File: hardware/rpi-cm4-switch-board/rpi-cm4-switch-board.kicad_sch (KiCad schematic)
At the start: 68 parts, among them J1 0826-1G1T-23-F, J2 0826-1G1T-23-F, J3 0826-1G1T-23-F, P1 USB_C_Plug_USB2.0, P2 USB_C_Plug_USB2.0, U3 74LVC1G07SE-7, U5 KSZ9567RTXI, U6 AP2127N-2.5, U7 AP2127N3-1.2

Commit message: Differential routing completed/roughed out. Schematic cleanup. More work to do on chip power pins.
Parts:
- removed CR1: SMBJ5.0A-TR, footprints:SMBJ5.0A-TR, symbol 2020-11-06_22-01-36:SMBJ5.0A-TR
- added C? (x27): 0.1uF, Capacitor_SMD:C_0402_1005Metric, symbol Device:C
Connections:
- net +3.3V: no longer U5.61 (VDDIO), U5.77 (VDDIO), U5.99 (VDDIO)
- net Cap5_D_P: now reaches C16.2, U5.120 (TXRX5P_D)
- net Cap5_C_P: now reaches C15.2, U5.117 (TXRX5P_C)
- net Cap4_C_N: now reaches C3.2, U5.40 (TXRX4M_C)
- net Cap4_B_P: now reaches C10.2, U5.37 (TXRX4P_B)
- net Cap5_A_N: now reaches C5.2, U5.113 (TXRX5M_A)
- net Cap4_D_N: now reaches C4.2, U5.43 (TXRX4M_D)
- net Cap5_A_P: now reaches C13.2, U5.112 (TXRX5P_A)
- net Cap4_A_N: now reaches C1.2, U5.35 (TXRX4M_A)
- net Cap4_C_P: now reaches C11.2, U5.39 (TXRX4P_C)
- net Cap5_C_N: now reaches C7.2, U5.118 (TXRX5M_C)
- net Cap5_B_P: now reaches C14.2, U5.115 (TXRX5P_B)
- net Cap5_B_N: now reaches C6.2, U5.116 (TXRX5M_B)
- net Cap5_D_N: now reaches C8.2, U5.121 (TXRX5M_D)
- net Cap4_A_P: now reaches C9.2, U5.34 (TXRX4P_A)
- net Cap4_B_N: now reaches C2.2, U5.38 (TXRX4M_B)
- net Cap4_D_P: now reaches C12.2, U5.42 (TXRX4P_D)
- net GPIO10: no longer names the net of Module2.44 (GPIO10)
- net GPIO10: no longer Module1.44 (GPIO10)
- net GPIO11: no longer names the net of Module2.38 (GPIO11)
- net GPIO11: no longer Module1.38 (GPIO11)
- net GPIO14: no longer names the net of Module2.55 (GPIO14)
- net GPIO14: no longer Module1.55 (GPIO14)
- net GPIO15: no longer names the net of Module2.51 (GPIO15)
- net GPIO15: no longer Module1.51 (GPIO15)
- net GPIO2: no longer names the net of Module2.58 (GPIO2)
- net GPIO2: no longer Module1.58 (GPIO2)
- net GPIO3: no longer names the net of Module2.56 (GPIO3)
- net GPIO3: no longer Module1.56 (GPIO3)
- net GPIO7: no longer names the net of Module2.37 (GPIO7)
- net GPIO7: no longer Module1.37 (GPIO7)
- net GPIO8: no longer names the net of Module2.39 (GPIO8)
- net GPIO8: no longer Module1.39 (GPIO8)
- net GPIO9: no longer names the net of Module2.40 (GPIO9)
- net GPIO9: no longer Module1.40 (GPIO9)
- now unconnected: U5.10 (AVDDH), U5.104 (DVDDL), U5.11 (DVDDL), U5.110 (DVDDL), U5.111 (AVDDH), U5.114 (AVDDL), U5.119 (AVDDL), U5.122 (AVDDH), U5.124 (AVDDL), U5.128 (AVDDH), U5.14 (AVDDL), U5.19 (AVDDL), U5.22 (AVDDH), U5.23 (DVDDL), U5.3 (AVDDL), U5.30 (AVDDL), U5.33 (AVDDH), U5.36 (AVDDL), U5.41 (AVDDL), U5.44 (AVDDH), U5.45 (DVDDL), U5.56 (DVDDL), U5.74 (DVDDL), U5.87 (DVDDL), U6.2 (VO), U7.2 (VO)
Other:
- moved on the sheet: C1, C10, C11, C12, C13, C14, C15, C16, C2, C3, C4, C5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

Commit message: Updated schematic symbol and footprint for ethernet chip, More work TBD
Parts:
- U? (x3): renamed from U5; value KSZ9567RTXI -> KSZ9567S; footprint library:QFP40P1600X1600X120-129N -> QFP40P1600X1600X120-129N; symbol KSZ9567RTXI:KSZ9567RTXI -> KSZ9567S:KSZ9567S
- gave numbers to parts that had none: 27
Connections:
- net +3.3V: now also U?.68 (VDDIO), U?.99 (VDDIO)
- net GND: now also U?.69 (GND), U?.75 (GND), U?.77 (GND), U?.80 (GND), U?.EPAD (GND); no longer U?.129 (GND), U?.46 (GND), U?.47 (GND), U?.84 (GND), U?.P1 (GND), U?.P10 (GND), U?.P11 (GND), U?.P12 (GND), U?.P13 (GND), U?.P14 (GND), U?.P15 (GND), U?.P16 (GND), U?.P17 (GND), U?.P18 (GND), U?.P19 (GND), U?.P2 (GND), U?.P20 (GND), U?.P21 (GND), U?.P22 (GND), U?.P23 (GND), U?.P24 (GND), U?.P25 (GND), U?.P26 (GND), U?.P27 (GND), U?.P28 (GND), U?.P29 (GND), U?.P3 (GND), U?.P30 (GND), U?.P31 (GND), U?.P32 (GND), U?.P33 (GND), U?.P34 (GND), U?.P35 (GND), U?.P36 (GND), U?.P37 (GND), U?.P38 (GND), U?.P39 (GND), U?.P4 (GND), U?.P40 (GND), U?.P41 (GND), U?.P42 (GND), U?.P43 (GND), U?.P44 (GND), U?.P45 (GND), U?.P48 (GND), U?.P49 (GND), U?.P5 (GND), U?.P50 (GND), U?.P51 (GND), U?.P52 (GND), U?.P53 (GND), U?.P54 (GND), U?.P55 (GND), U?.P56 (GND), U?.P57 (GND), U?.P58 (GND), U?.P59 (GND), U?.P6 (GND), U?.P60 (GND), U?.P61 (GND), U?.P62 (GND), U?.P63 (GND), U?.P64 (GND), U?.P7 (GND), U?.P8 (GND), U?.P9 (GND)
- net 1.2V: now reaches U7.2 (VO)
- net 1.2V: now also U?.104 (DVDDL), U?.11 (DVDDL), U?.110 (DVDDL), U?.114 (AVDDL), U?.119 (AVDDL), U?.124 (AVDDL), U?.14 (AVDDL), U?.19 (AVDDL), U?.23 (DVDDL), U?.3 (AVDDL), U?.30 (AVDDL), U?.36 (AVDDL), U?.41 (AVDDL), U?.45 (DVDDL), U?.56 (DVDDL), U?.66 (DVDDL), U?.70 (DVDDL), U?.71 (VDDLS), U?.84 (VDDLS), U?.87 (DVDDL)
- net 2.5V: now reaches U?.10 (AVDDH)
- net 2.5V: now also U6.2 (VO), U?.111 (AVDDH), U?.122 (AVDDH), U?.128 (AVDDH), U?.22 (AVDDH), U?.33 (AVDDH), U?.44 (AVDDH), U?.72 (VDDHS), U?.83 (VDDHS)
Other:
- moved on the sheet: C17, C18, C19, C20, C21, C22, C23, C24, C25, C26, C27, C28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

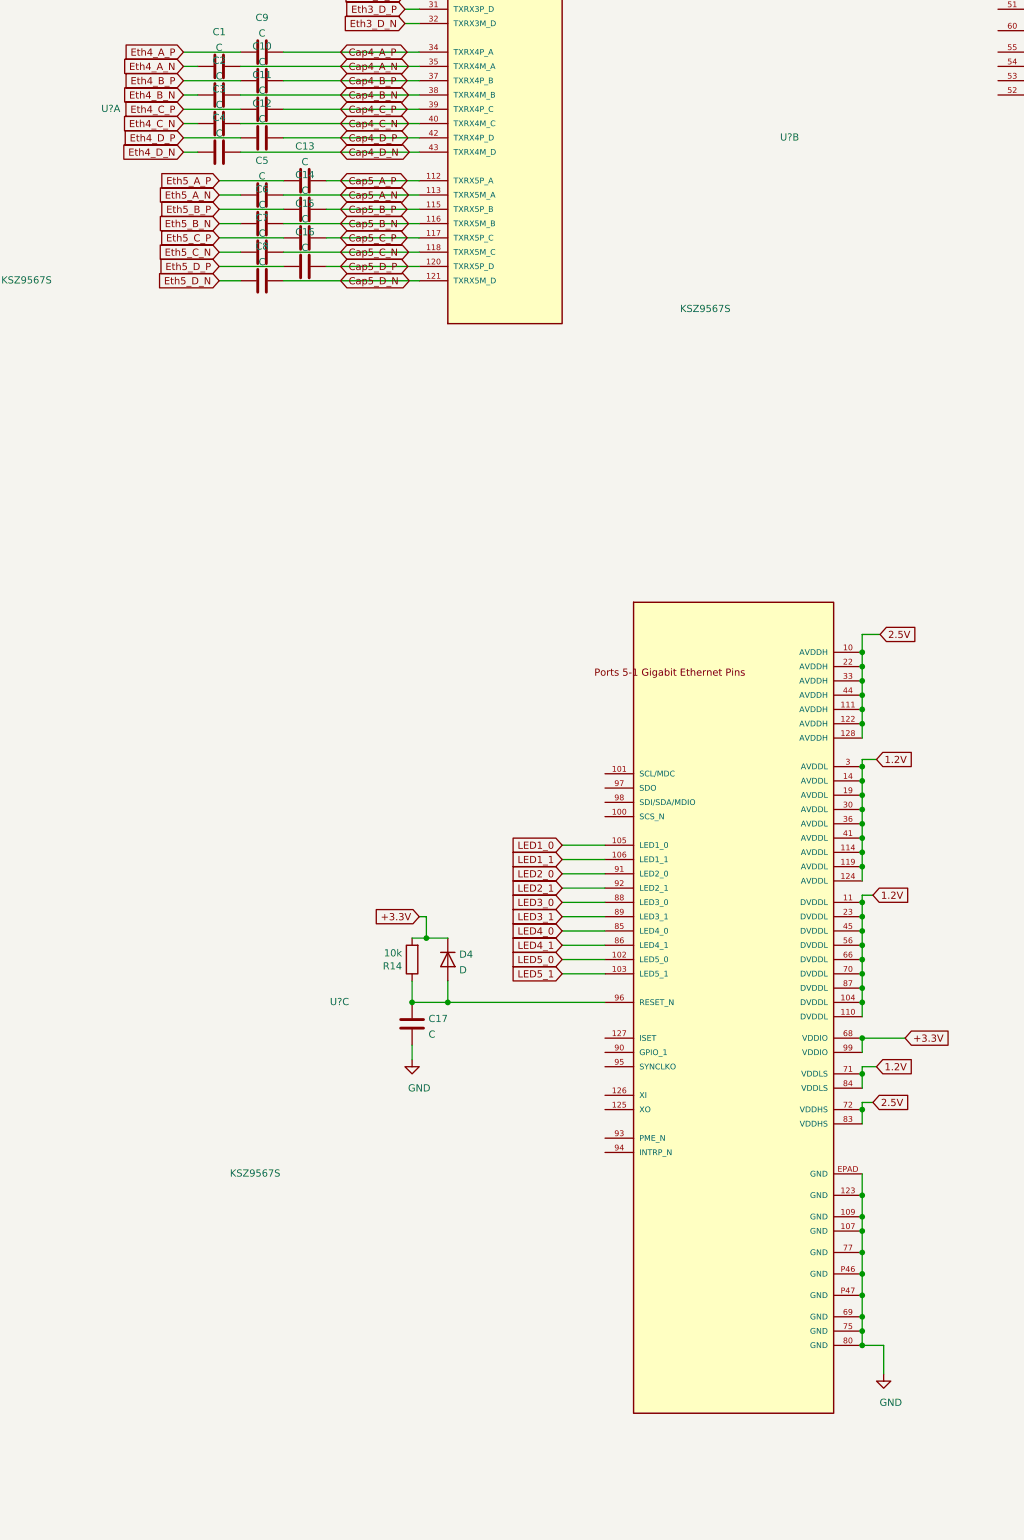
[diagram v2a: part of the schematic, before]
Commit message: Updated KSZ9567 symbol. Went through full pin list and fixed a few missing pin definitions.
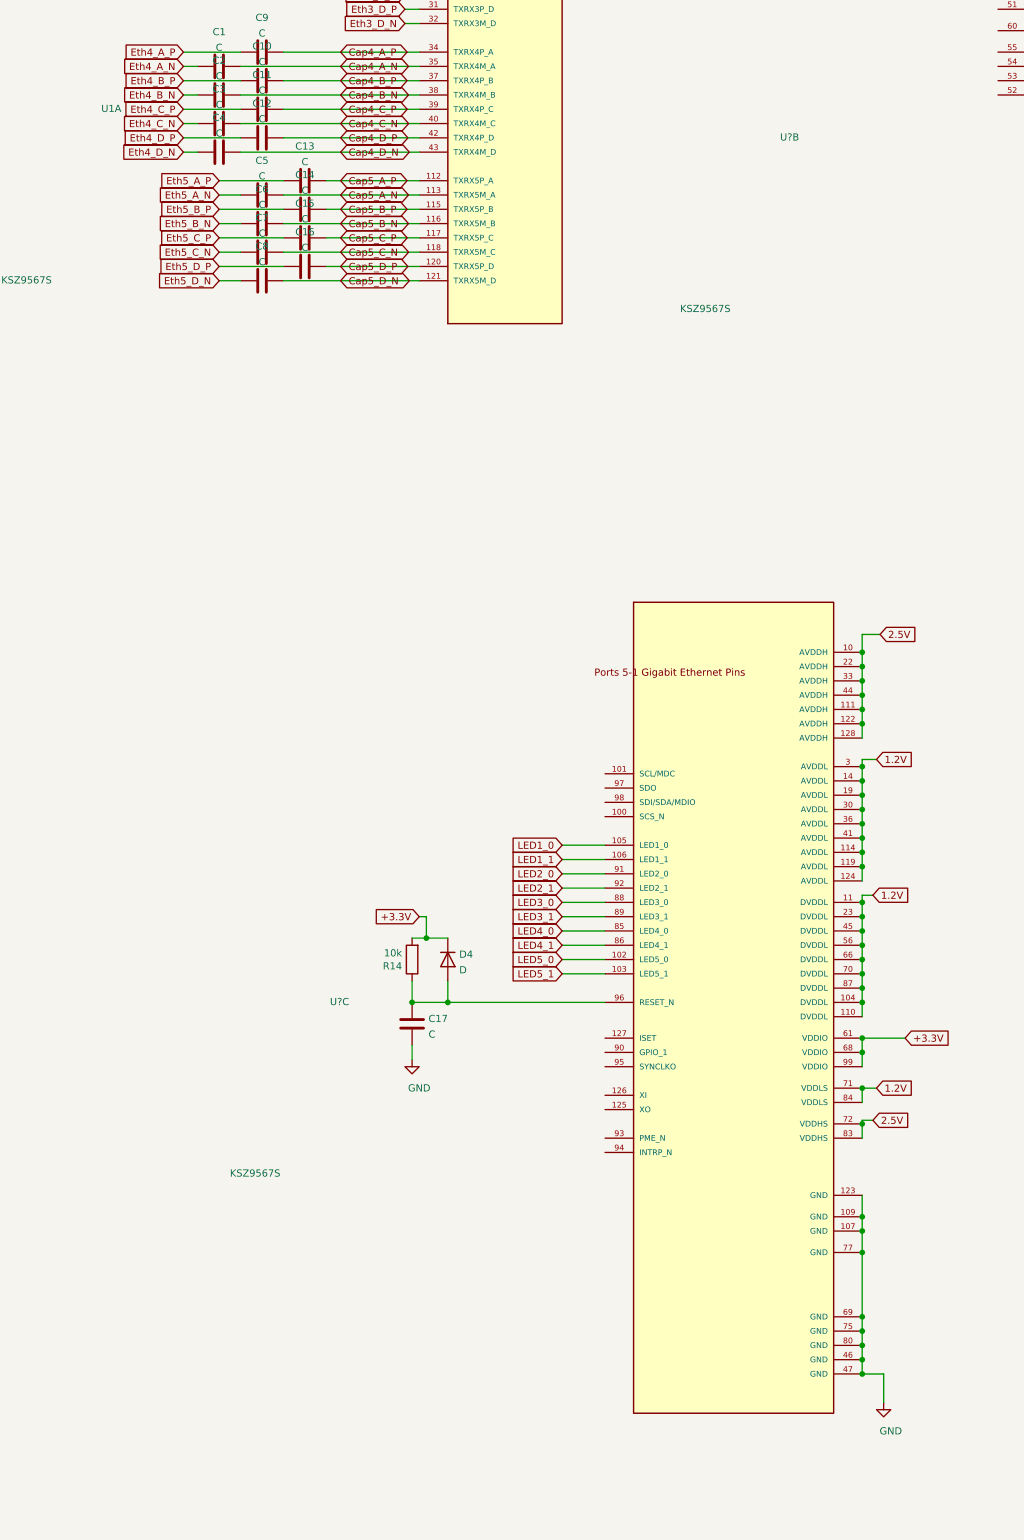
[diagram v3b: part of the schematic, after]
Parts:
- gave numbers to parts that had none: 1
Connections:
- net +3.3V: now also U?.61 (VDDIO)
- net GND: now also U?.46 (GND), U?.47 (GND); no longer U?.EPAD (GND), U?.P46 (GND), U?.P47 (GND)
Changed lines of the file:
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@@
   (junction (at 438.15 95.25) (diameter 1.016) (color 0 0 0 0))
   (junction (at 438.15 101.6) (diameter 1.016) (color 0 0 0 0))
-  (junction (at 438.15 107.95) (diameter 1.016) (color 0 0 0 0))
-  (junction (at 438.15 114.3) (diameter 1.016) (color 0 0 0 0))
-  (junction (at 438.15 129.54) (diameter 1.016) (color 0 0 0 0))
+  (junction (at 438.15 104.14) (diameter 1.016) (color 0 0 0 0))
+  (junction (at 438.15 110.49) (diameter 1.016) (color 0 0 0 0))
+  (junction (at 438.15 116.84) (diameter 1.016) (color 0 0 0 0))
   (junction (at 438.15 133.35) (diameter 1.016) (color 0 0 0 0))
   (junction (at 438.15 135.89) (diameter 1.016) (color 0 0 0 0))
   (junction (at 438.15 139.7) (diameter 1.016) (color 0 0 0 0))
-  (junction (at 438.15 143.51) (diameter 1.016) (color 0 0 0 0))
-  (junction (at 438.15 147.32) (diameter 1.016) (color 0 0 0 0))
   (junction (at 438.15 151.13) (diameter 1.016) (color 0 0 0 0))
   (junction (at 438.15 153.67) (diameter 1.016) (color 0 0 0 0))
   (junction (at 438.15 156.21) (diameter 1.016) (color 0 0 0 0))
+  (junction (at 438.15 158.75) (diameter 1.016) (color 0 0 0 0))
+  (junction (at 438.15 161.29) (diameter 1.016) (color 0 0 0 0))
   (junction (at 514.985 53.34) (diameter 1.016) (color 0 0 0 0))
   (no_connect (at 168.91 -144.78))
@@
     (stroke (width 0) (type solid) (color 0 0 0 0))
   )
-  (wire (pts (xy 438.15 106.68) (xy 438.15 107.95))
+  (wire (pts (xy 438.15 104.14) (xy 438.15 106.68))
     (stroke (width 0) (type solid) (color 0 0 0 0))
   )
-  (wire (pts (xy 438.15 107.95) (xy 438.15 110.49))
+  (wire (pts (xy 438.15 110.49) (xy 438.15 113.03))
     (stroke (width 0) (type solid) (color 0 0 0 0))
   )
-  (wire (pts (xy 438.15 113.03) (xy 438.15 114.3))
+  (wire (pts (xy 438.15 110.49) (xy 440.69 110.49))
     (stroke (width 0) (type solid) (color 0 0 0 0))
   )
-  (wire (pts (xy 438.15 114.3) (xy 438.15 116.84))
+  (wire (pts (xy 438.15 116.205) (xy 438.15 116.84))
     (stroke (width 0) (type solid) (color 0 0 0 0))
   )
-  (wire (pts (xy 438.15 125.73) (xy 438.15 129.54))
+  (wire (pts (xy 438.15 116.84) (xy 438.15 119.38))
     (stroke (width 0) (type solid) (color 0 0 0 0))
   )
@@
     (stroke (width 0) (type solid) (color 0 0 0 0))
   )
-  (wire (pts (xy 438.15 139.7) (xy 438.15 143.51))
+  (wire (pts (xy 438.15 139.7) (xy 438.15 151.13))
     (stroke (width 0) (type solid) (color 0 0 0 0))
   )
-  (wire (pts (xy 438.15 143.51) (xy 438.15 147.32))
+  (wire (pts (xy 438.15 151.13) (xy 438.15 153.67))
     (stroke (width 0) (type solid) (color 0 0 0 0))
   )
-  (wire (pts (xy 438.15 147.32) (xy 438.15 151.13))
+  (wire (pts (xy 438.15 153.67) (xy 438.15 156.21))
     (stroke (width 0) (type solid) (color 0 0 0 0))
   )
-  (wire (pts (xy 438.15 151.13) (xy 438.15 153.67))
+  (wire (pts (xy 438.15 156.21) (xy 438.15 158.75))
     (stroke (width 0) (type solid) (color 0 0 0 0))
   )
-  (wire (pts (xy 438.15 153.67) (xy 438.15 156.21))
+  (wire (pts (xy 438.15 158.75) (xy 438.15 161.29))
     (stroke (width 0) (type solid) (color 0 0 0 0))
   )
-  (wire (pts (xy 438.15 156.21) (xy 441.96 156.21))
+  (wire (pts (xy 438.15 161.29) (xy 441.96 161.29))
     (stroke (width 0) (type solid) (color 0 0 0 0))
   )
@@
     (stroke (width 0) (type solid) (color 0 0 0 0))
   )
-  (wire (pts (xy 440.055 113.03) (xy 438.15 113.03))
+  (wire (pts (xy 440.055 116.205) (xy 438.15 116.205))
     (stroke (width 0) (type solid) (color 0 0 0 0))
   )
@@
     (stroke (width 0) (type solid) (color 0 0 0 0))
   )
-  (wire (pts (xy 440.69 106.68) (xy 438.15 106.68))
-    (stroke (width 0) (type solid) (color 0 0 0 0))
-  )
   (wire (pts (xy 441.325 29.845) (xy 438.15 29.845))
     (stroke (width 0) (type solid) (color 0 0 0 0))
   )
-  (wire (pts (xy 441.96 156.21) (xy 441.96 161.29))
+  (wire (pts (xy 441.96 161.29) (xy 441.96 166.37))
     (stroke (width 0) (type solid) (color 0 0 0 0))
   )
@@
     )
   )
-  (global_label "2.5V" (shape input) (at 440.055 113.03 0) (fields_autoplaced)
+  (global_label "2.5V" (shape input) (at 440.055 116.205 0) (fields_autoplaced)
     (effects (font (size 1.27 1.27)) (justify left))
-    (property "Intersheet References" "${INTERSHEET_REFS}" (id 0) (at 446.5805 113.1094 0)
+    (property "Intersheet References" "${INTERSHEET_REFS}" (id 0) (at 446.5805 116.2844 0)
       (effects (font (size 1.27 1.27)) (justify left) hide)
     )
@@
     )
   )
-  (global_label "1.2V" (shape input) (at 440.69 106.68 0) (fields_autoplaced)
+  (global_label "1.2V" (shape input) (at 440.69 110.49 0) (fields_autoplaced)
     (effects (font (size 1.27 1.27)) (justify left))
-    (property "Intersheet References" "${INTERSHEET_REFS}" (id 0) (at 447.2155 106.6006 0)
+    (property "Intersheet References" "${INTERSHEET_REFS}" (id 0) (at 447.2155 110.4106 0)
       (effects (font (size 1.27 1.27)) (justify left) hide)
     )
@@
     (pin "1")
   )
-  (symbol (lib_id "power:GND") (at 441.96 161.29 0) (unit 1)
+  (symbol (lib_id "power:GND") (at 441.96 166.37 0) (unit 1)
     (in_bom yes) (on_board yes)
-    (property "Reference" "#PWR020" (id 0) (at 441.96 167.64 0)
+    (property "Reference" "#PWR020" (id 0) (at 441.96 172.72 0)
       (effects (font (size 1.27 1.27)) hide)
     )
-    (property "Value" "GND" (id 1) (at 443.23 166.37 0))
-    (property "Footprint" "" (id 2) (at 441.96 161.29 0)
+    (property "Value" "GND" (id 1) (at 443.23 171.45 0))
+    (property "Footprint" "" (id 2) (at 441.96 166.37 0)
       (effects (font (size 1.27 1.27)) hide)
     )
-    (property "Datasheet" "" (id 3) (at 441.96 161.29 0)
+    (property "Datasheet" "" (id 3) (at 441.96 166.37 0)
       (effects (font (size 1.27 1.27)) hide)
     )
@@
     (pin "S2")
   )
-  (symbol (lib_id "KSZ9567S:KSZ9567S") (at 495.3 -81.28 0) (unit 2)
+  (symbol (lib_name "KSZ9567S_1") (lib_id "KSZ9567S:KSZ9567S") (at 495.3 -81.28 0) (unit 2)
     (in_bom yes) (on_board yes)
     (property "Reference" "U?" (id 0) (at 423.545 -57.785 0)
@@
   (symbol (lib_id "KSZ9567S:KSZ9567S") (at 374.65 -86.36 0) (unit 1)
     (in_bom yes) (on_board yes) (fields_autoplaced)
-    (property "Reference" "U?" (id 0) (at 302.895 -62.865 0)
+    (property "Reference" "U1" (id 0) (at 302.895 -62.865 0)
       (effects (font (size 1.27 1.27)) (justify left bottom))
     )
@@
     (pin "9")
   )
-  (symbol (lib_id "KSZ9567S:KSZ9567S") (at 415.29 72.39 0) (unit 3)
+  (symbol (lib_name "KSZ9567S_2") (lib_id "KSZ9567S:KSZ9567S") (at 415.29 72.39 0) (unit 3)
     (in_bom yes) (on_board yes) (fields_autoplaced)
     (property "Reference" "U?" (id 0) (at 343.535 95.885 0)
@@
     (pin "44")
     (pin "45")
+    (pin "46")
+    (pin "47")
     (pin "56")
+    (pin "61")
     (pin "66")
     (pin "68")
@@
     (pin "98")
     (pin "99")
-    (pin "EPAD")
-    (pin "P46")
-    (pin "P47")
   )
   (symbol (lib_id "CM4IO:ComputeModule4-CM4") (at 59.69 -88.9 0) (unit 1)
@@
       (reference "R18") (unit 1) (value "50") (footprint "Resistor_SMD:R_0603_1608Metric")
     )
+    (path "/74a36cd2-9679-4680-8faa-902a33c55144"
+      (reference "U1") (unit 1) (value "KSZ9567S") (footprint "QFP40P1600X1600X120-129N")
+    )
     (path "/2e2b98f0-9f13-4566-93b5-98deb93a1fa4"
       (reference "U3") (unit 1) (value "74LVC1G07SE-7") (footprint "Package_TO_SOT_SMD:SOT-353_SC-70-5")
@@
       (reference "U7") (unit 1) (value "AP2127N3-1.2") (footprint "Package_TO_SOT_SMD:TSOT-23")
     )
-    (path "/74a36cd2-9679-4680-8faa-902a33c55144"
-      (reference "U?") (unit 1) (value "KSZ9567S") (footprint "QFP40P1600X1600X120-129N")
-    )
     (path "/2e10adaa-940c-41dd-b280-4d6528ef1d58"
